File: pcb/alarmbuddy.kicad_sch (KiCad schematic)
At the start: 30 parts, among them J1 24VAC, J2 3V3, J3 SENS1-3, J4 SENS4-6, J5 SENS7-9, J6 SENS10-12, J7 eflashy32, U1 BD9G101G, U2 ESP32-S2-WROVER

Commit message: fix programmer mixup with gpio0 :(
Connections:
- net RTS renamed EN
- net EN: now also J7.5 (Pin_5); no longer J7.6 (Pin_6)
- net ~{DTR} renamed GPIO0
- net GPIO0: now also J7.6 (Pin_6); no longer J7.5 (Pin_5)
- no-connect marks 2 -> 16
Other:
- note removed: "Confirm fuse sizing depending on input voltage. (eg. 5VDC need bigger fuse)"
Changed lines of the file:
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@@
   (junction (at 242.57 71.12) (diameter 0) (color 0 0 0 0)
   )
+  (no_connect (at 247.65 124.46))
   (no_connect (at 247.65 91.44))
+  (no_connect (at 247.65 114.3))
   (no_connect (at 247.65 88.9))
+  (no_connect (at 247.65 116.84))
+  (no_connect (at 247.65 119.38))
+  (no_connect (at 247.65 101.6))
+  (no_connect (at 247.65 129.54))
+  (no_connect (at 247.65 121.92))
+  (no_connect (at 247.65 104.14))
+  (no_connect (at 247.65 109.22))
+  (no_connect (at 247.65 127))
+  (no_connect (at 247.65 106.68))
+  (no_connect (at 247.65 132.08))
+  (no_connect (at 247.65 99.06))
+  (no_connect (at 247.65 111.76))
+  (polyline (pts (xy 17.78 20.32) (xy 195.58 20.32))
+    (stroke (width 0) (type default) (color 0 0 0 0))
+  )
   (wire (pts (xy 41.275 29.21) (xy 47.625 29.21))
     (stroke (width 0) (type default) (color 0 0 0 0))
@@
     (stroke (width 0) (type default) (color 0 0 0 0))
   )
+  (polyline (pts (xy 195.58 20.32) (xy 195.58 64.77))
+    (stroke (width 0) (type default) (color 0 0 0 0))
+  )
   (wire (pts (xy 62.23 33.655) (xy 63.5 33.655))
     (stroke (width 0) (type default) (color 0 0 0 0))
@@
     (stroke (width 0) (type default) (color 0 0 0 0))
   )
-  (polyline (pts (xy 17.145 19.685) (xy 155.575 19.685))
-    (stroke (width 0) (type default) (color 0 0 0 0))
-  )
   (wire (pts (xy 47.625 22.86) (xy 63.5 22.86))
     (stroke (width 0) (type default) (color 0 0 0 0))
@@
     (stroke (width 0) (type default) (color 0 0 0 0))
   )
-  (polyline (pts (xy 17.145 19.685) (xy 17.145 51.435))
-    (stroke (width 0) (type default) (color 0 0 0 0))
-  )
   (wire (pts (xy 163.83 36.83) (xy 163.83 33.02))
     (stroke (width 0) (type default) (color 0 0 0 0))
@@
     (stroke (width 0) (type default) (color 0 0 0 0))
   )
-  (polyline (pts (xy 207.01 118.11) (xy 203.2 118.11))
-    (stroke (width 0) (type default) (color 0 0 0 0))
-  )
   (wire (pts (xy 148.59 55.88) (xy 151.13 55.88))
     (stroke (width 0) (type default) (color 0 0 0 0))
@@
     (stroke (width 0) (type default) (color 0 0 0 0))
   )
+  (polyline (pts (xy 195.58 64.77) (xy 17.78 64.77))
+    (stroke (width 0) (type default) (color 0 0 0 0))
+  )
   (wire (pts (xy 232.41 71.12) (xy 232.41 83.82))
     (stroke (width 0) (type default) (color 0 0 0 0))
@@
     (stroke (width 0) (type default) (color 0 0 0 0))
   )
+  (polyline (pts (xy 17.78 20.32) (xy 17.78 64.77))
+    (stroke (width 0) (type default) (color 0 0 0 0))
+  )
   (wire (pts (xy 144.78 36.195) (xy 144.78 33.02))
     (stroke (width 0) (type default) (color 0 0 0 0))
@@
     (stroke (width 0) (type default) (color 0 0 0 0))
   )
-  (text "Confirm fuse sizing depending\non input voltage. \n(eg. 5VDC need bigger fuse)"
-    (at 20.32 45.72 0)
-    (effects (font (size 1.27 1.27)) (justify left bottom))
-  )
-  (text "GPIO11-18 = ADC2\nMust disable WiFi for ADC2" (at 196.85 124.46 180)
+  (text "GPIO11-18 = ADC2\nMust disable WiFi for ADC2" (at 205.74 121.92 180)
     (effects (font (size 1.27 1.27)) (justify right bottom))
   )
@@
     (effects (font (size 0.6096 0.6096)) (justify left bottom))
   )
-  (text "24VAC->3.3VDC Regulation (500mA max)" (at 17.78 18.415 0)
+  (text "24VAC->3.3VDC Regulation (500mA max)" (at 20.32 19.05 0)
     (effects (font (size 1.27 1.27)) (justify left bottom))
   )
   (text "GPIO18 works as U1RXD and is in\n an uncertain state when the chip is powered on, \nwhich may affect the chip’s\nentry into download boot mode. \nTo solve this issue, add an \nexternal pull-up resistor."
-    (at 207.01 154.94 180)
+    (at 200.66 137.16 180)
     (effects (font (size 1.27 1.27)) (justify right bottom))
   )
@@
     (effects (font (size 0.9906 0.9906)) (justify right bottom))
   )
-  (label "~{DTR}" (at 29.21 148.59 0)
+  (label "EN" (at 29.21 148.59 0)
     (effects (font (size 0.9906 0.9906)) (justify left bottom))
   )
-  (label "RTS" (at 29.21 146.05 0)
+  (label "GPIO0" (at 29.21 146.05 0)
     (effects (font (size 0.9906 0.9906)) (justify left bottom))
   )
@@
     (effects (font (size 1.27 1.27)) (justify left bottom))
   )
-  (label "~{DTR}" (at 217.17 91.44 180)
-    (effects (font (size 0.9906 0.9906)) (justify right bottom))
-  )
-  (label "RTS" (at 212.09 88.9 180)
-    (effects (font (size 0.9906 0.9906)) (justify right bottom))
-  )
+  (label "GPIO0" (at 217.17 91.44 180)
+    (effects (font (size 0.9906 0.9906)) (justify right bottom))
+  )
+  (label "EN" (at 212.09 88.9 180)
+    (effects (font (size 0.9906 0.9906)) (justify right bottom))
+  )

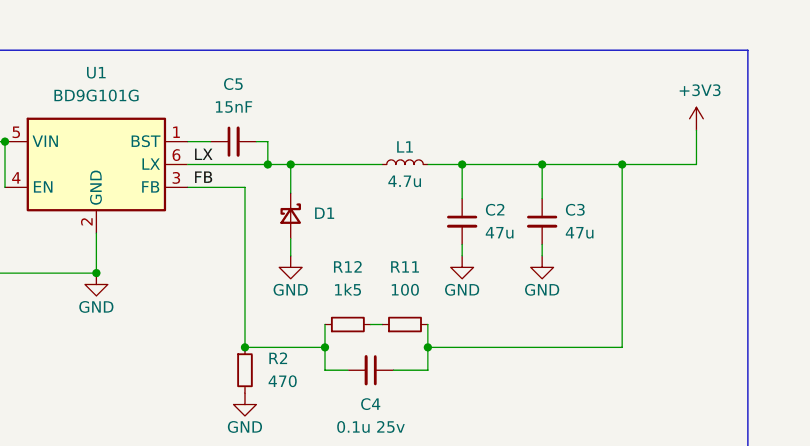
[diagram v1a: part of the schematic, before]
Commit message: kicad v7 and render
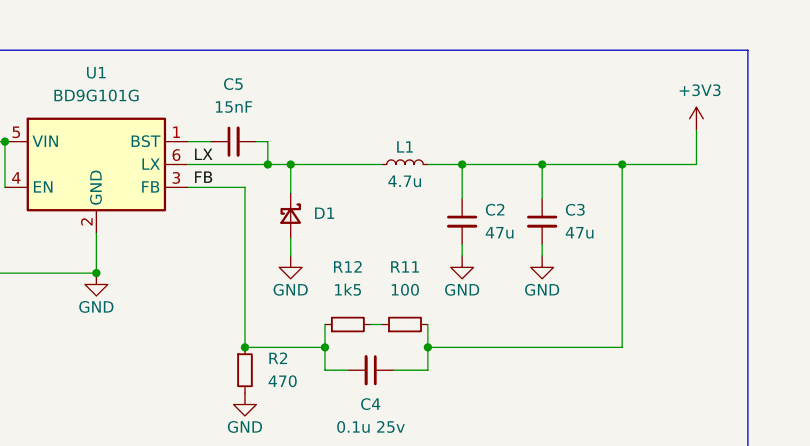
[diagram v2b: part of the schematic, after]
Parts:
- L1: footprint switching:L_Sunlord_MWSA0402_4.4x4.2mm -> Inductor_SMD:L_Sunlord_MWSA0402S
